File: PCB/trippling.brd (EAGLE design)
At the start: 60 x 41 mm, 24 parts, among them K1 RELAY-SPDT-JZC-11F, K2 RELAY-SPDT-JZC-11F, T1 MMBT3904, T2 MMBT3904, X1 1751277

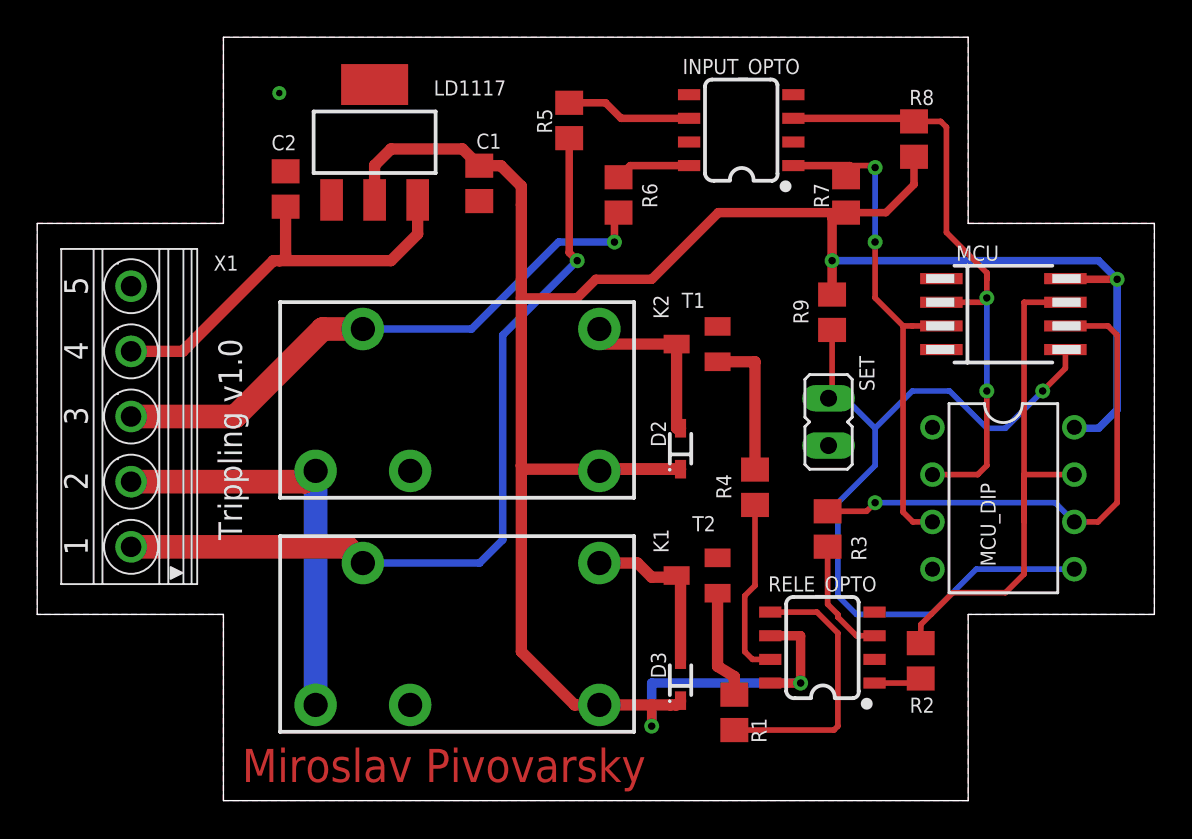
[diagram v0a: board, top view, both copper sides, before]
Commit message: Fix HW pinout Fix SW pinout add documentation for AVR dragon
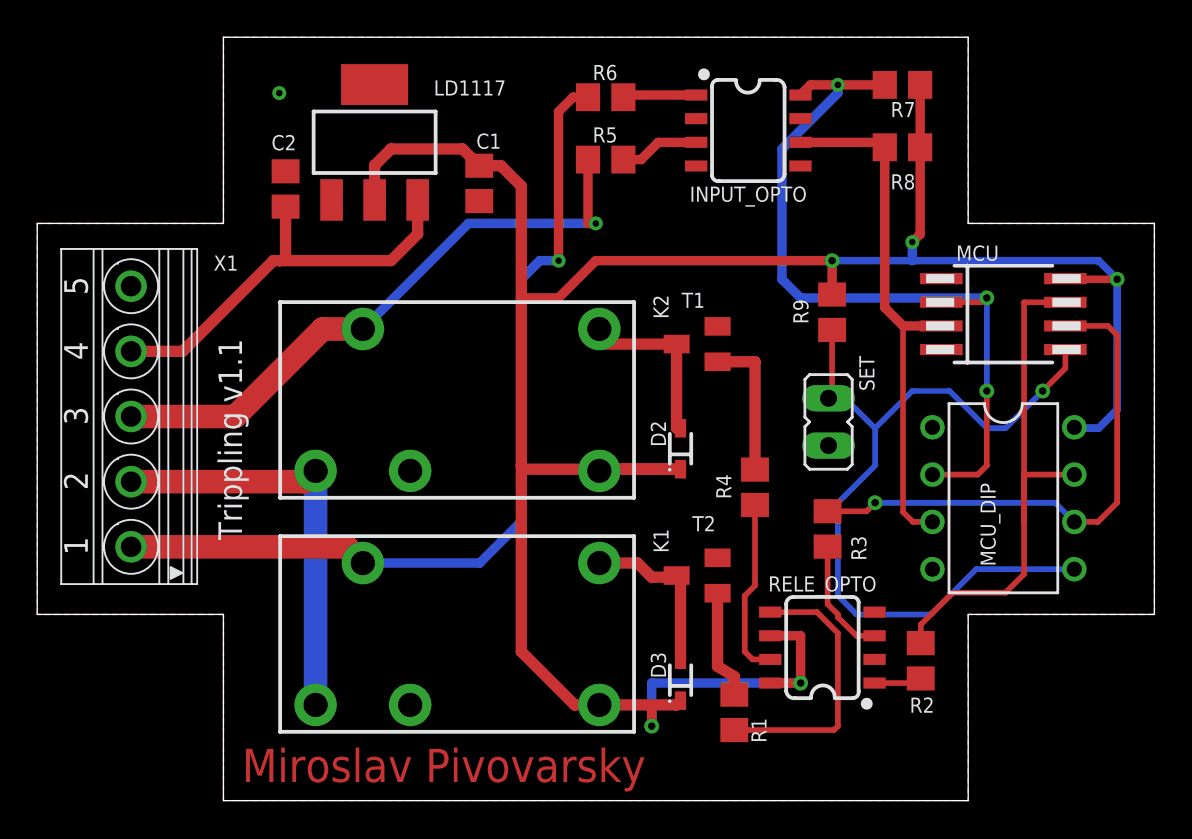
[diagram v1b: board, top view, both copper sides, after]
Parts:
- R2, R3: value 470 -> 120
- R7, R8, R9: value 470 -> 10k
- moved R7 6.64 mm to (46.5, 38.4), turned to 0 degrees
- moved R6 5.30 mm to (30.5, 37.8), turned to 180 degrees
- moved R5 2.87 mm to (30.5, 34.4), turned to 180 degrees
- moved R8 0.76 mm to (46.5, 35.1), turned to 0 degrees
- moved INPUT_OPTO 0.38 mm to (38.2, 36.0), turned to 270 degrees
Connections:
- removed net N$5: INPUT_OPTO.6, R5.1
- removed net N$6: INPUT_OPTO.8, R6.1
- new net N$1: INPUT_OPTO.1, R6.1
- new net N$2: INPUT_OPTO.3, R5.1
- net I_LEFT: now also INPUT_OPTO.6, R8.1; no longer INPUT_OPTO.1, R7.1
- net I_RIGHT: now also INPUT_OPTO.8, R7.1; no longer INPUT_OPTO.3, R8.1
- net LEFT: now also R6.2; no longer R5.2
- net RIGHT: now also R5.2; no longer R6.2
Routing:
- net I_RIGHT: track 33.5 -> 42.5 mm, vias 2 -> 3
- net N$5: track 6.79 -> 0.00 mm
- net N$2: track 0.00 -> 4.29 mm
- net N$6: track 4.05 -> 0.00 mm
- net N$1: track 0.00 -> 3.96 mm
- net LEFT: track 44.2 -> 47.6 mm
- net RIGHT: track 31.5 -> 33.1 mm
- net +5V: track 134.5 -> 133.9 mm, vias 4 -> 5
- net I_LEFT: track 28.3 -> 28.5 mm, vias 2 -> 0
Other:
- board text added: "Trippling v1.1"
- board text removed: "Trippling v1.0"
